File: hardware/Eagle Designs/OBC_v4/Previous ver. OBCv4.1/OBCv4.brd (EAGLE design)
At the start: 90.2 x 95.5 mm, 35 parts, among them J1 MOLEX_503763-0491MOLEX_503763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, J10 503763-0591, J11 503763-0591, J12 503763-0691, J13 MOLEX_503763-0291MOLEX_503763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, J16 U.FL-R-SMT-1(01), J2 MOLEX_503763-0491MOLEX_503763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, J6 MOLEX_503763-0491MOLEX_503763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, J9 U.FL-R-SMT-1(01), P8 SSW-123-02-G-D, P9 SSW-123-02-G-D, U1 TMP36FSZR_8_ADI-L, U2 LTC1477CS8LINEAR_TECHNOLOGY_L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, U3 RFM69HCW_433_900, U6 ORION_A38LORION_A38L, U7 PA1010D, X1 C25582-40G-M36-0A, X2 SSW-120-02-G-D

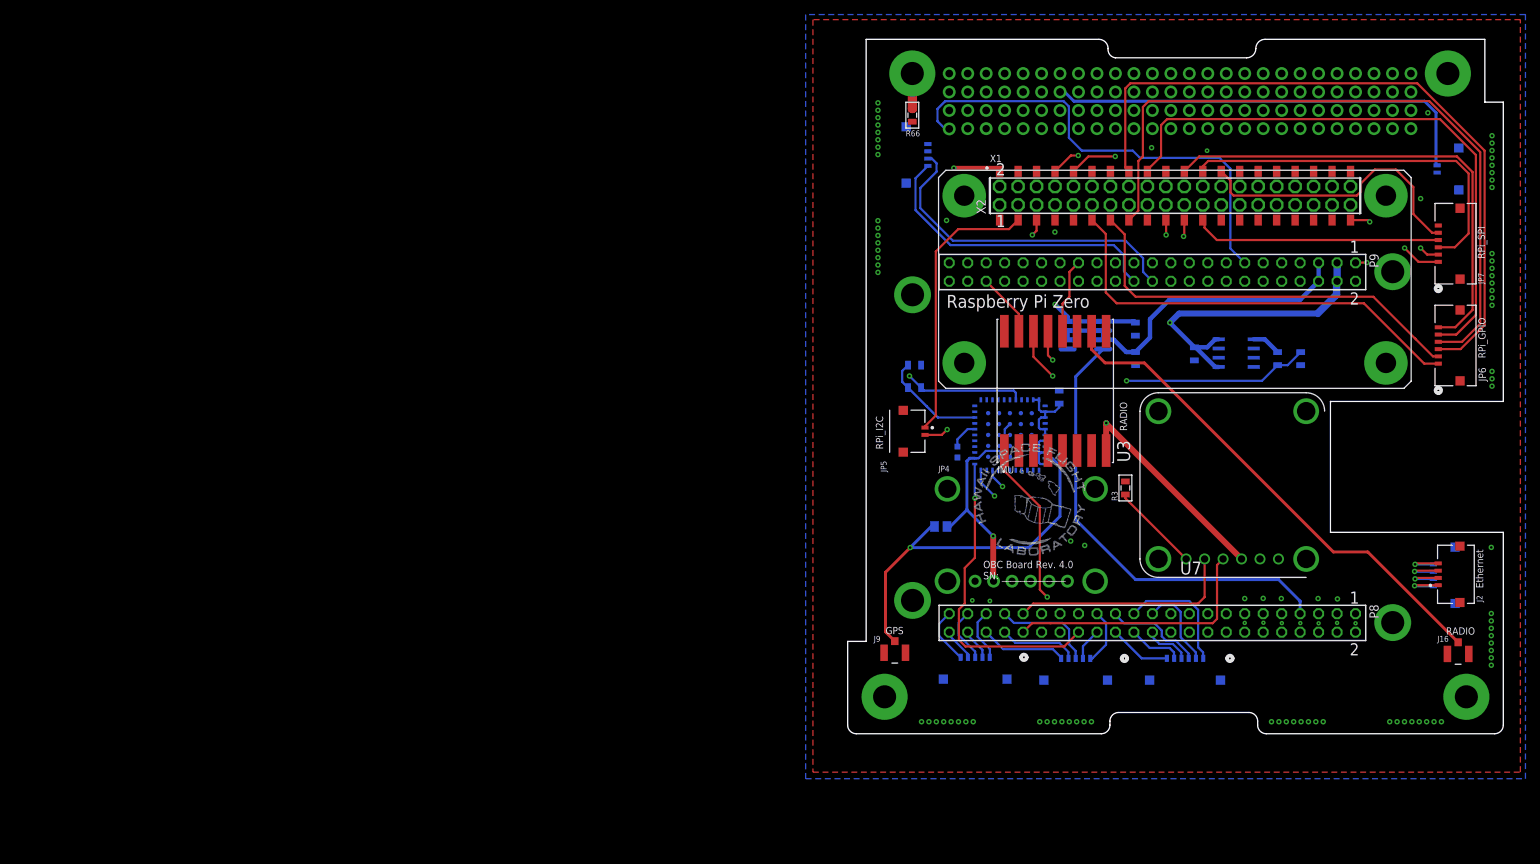
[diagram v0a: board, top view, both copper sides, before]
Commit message: updated OBC v4.1; verified & updated Battery Charging Circuit
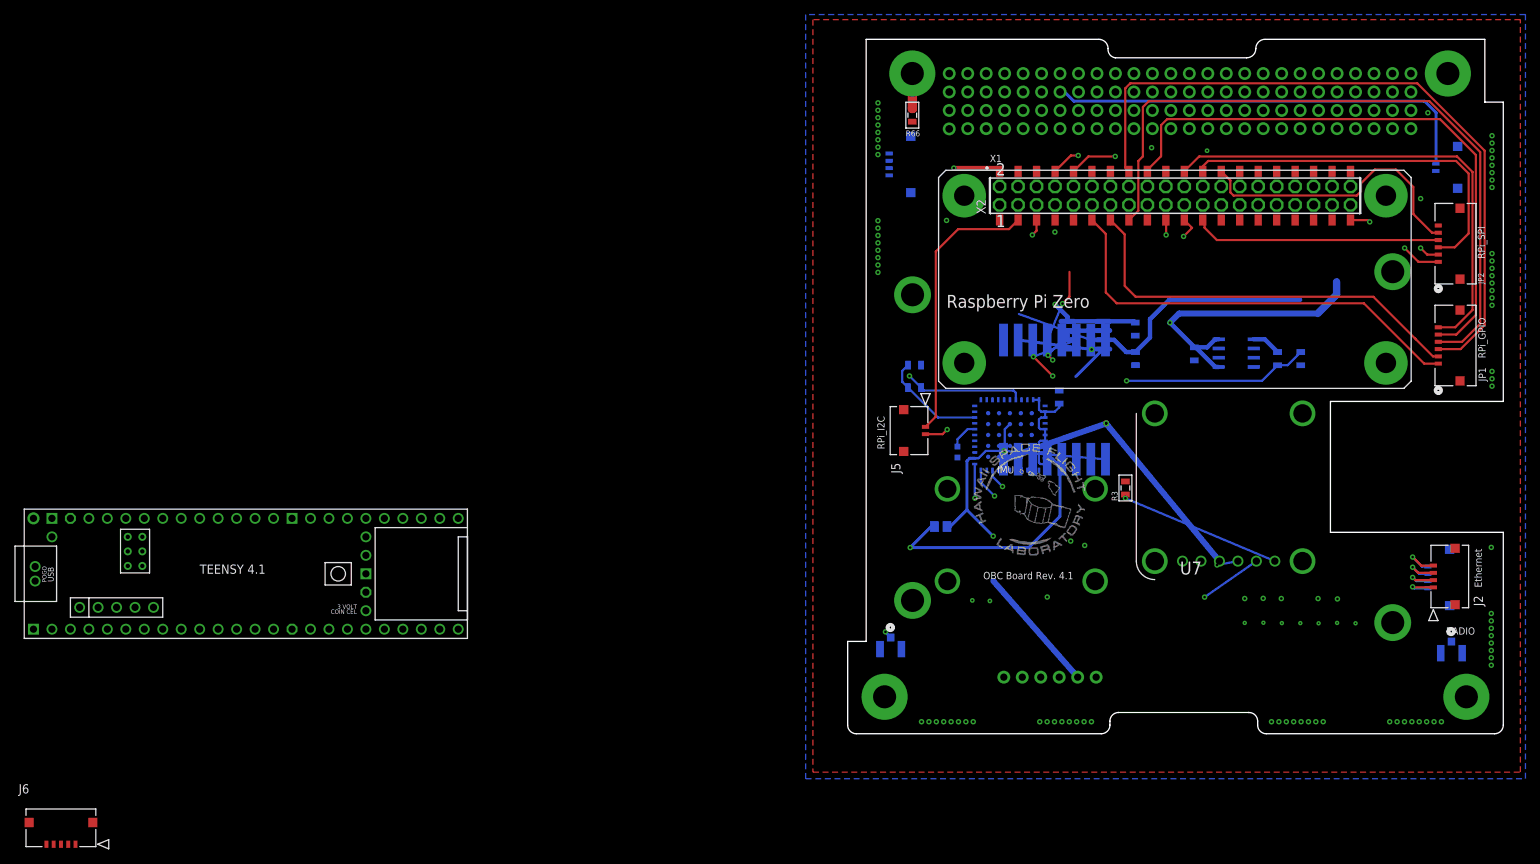
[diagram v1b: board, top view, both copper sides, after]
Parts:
- removed J10, J11: 503763-0591, Improved Molex 503763-0591:CONN_5037630591_MOL
- removed J12: 503763-0691, Improved Molex 503763-0691:CONN_503763-0691_MOL
- removed J13, JP5: MOLEX_503763-0291MOLEX_503763-0291_0_0, Molex - 503763-0291:MOLEX_503763-0291_0
- removed P8, P9: SSW-123-02-G-D, con-samtec:SSW-123-02-G-D
- added J3, J5: 5037630291, OBCv4:CON_5037630291
- added J4: 5037630491, OBCv4:CON_5037630491
- added U$1: TEENSY41, OBCv4:TEENSY41
- C1: value .1uF -> 0.1 uF
- C2, C3: value 1uF -> 1 uF
- J1, J2: value MOLEX_503763-0491MOLEX_503763-0491_0_0 -> 5037630491; device Molex - 503763-0491:MOLEX_503763-0491_0 -> OBCv4:CON_5037630491
- J6: value MOLEX_503763-0491MOLEX_503763-0491_0_0 -> 5037630591; device Molex - 503763-0491:MOLEX_503763-0491_0 -> OBCv4:CON_5037630591
- R1: value 27k -> 45.3k
- moved J6 148.9 mm to (-106.2, -15.2), flipped to the top, turned to 0 degrees
- moved JP4 13.8 mm to (27.8, 7.78), flipped to the bottom
- moved J2 3.58 mm to (80.6, 20.1)
- moved J1 3.42 mm to (79.8, 23.0)
- moved U3 1.20 mm to (28.4, 46.0), flipped to the bottom
- moved J16 0.93 mm to (83.0, 11.1), flipped to the bottom
- moved J9 0.75 mm to (5.92, 11.6), flipped to the bottom
- moved U7 0.58 mm to (52.4, 33.9), flipped to the bottom
- renumbered JP6 to JP1, JP7 to JP2
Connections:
- removed net AGND: P9.34
- removed net BUS_UART4_RXD(BBB_TX): H1.1.1, P9.13
- removed net BUS_UART4_TXD(BBB_RX): H1.1.2, P9.11
- removed net GPIO0_27: P8.17
- removed net GPIO1_0: J12.1, P8.25
- removed net GPIO1_1: J12.4, P8.24
- removed net GPIO1_12: P8.12
- removed net GPIO1_13: P8.11
- removed net GPIO1_14: P8.16
- removed net GPIO1_15: P8.15
- removed net GPIO1_16: P9.15
- removed net GPIO1_17: P9.23
- removed net GPIO1_2: P8.5
- removed net GPIO1_28: P9.12
- removed net GPIO1_29: J12.5, P8.26
- removed net GPIO1_3: P8.6
- removed net GPIO1_30: P8.21
- removed net GPIO1_31: P8.20
- removed net GPIO1_4: J12.2, P8.23
- removed net GPIO1_6: P8.3
- removed net GPIO1_7: P8.4
- removed net GPIO2_1: P8.18
- removed net GPIO2_10: J10.1, P8.41
- removed net GPIO2_11: J11.5, P8.42
- removed net GPIO2_12: J11.3, P8.39
- removed net GPIO2_13: J11.4, P8.40
- removed net GPIO2_22: J12.3, P8.27
- removed net GPIO2_23: J11.1, P8.29
- removed net GPIO2_24: J12.6, P8.28
- removed net GPIO2_25: J11.2, P8.30
- removed net GPIO2_6: J10.5, P8.45
- removed net GPIO2_7: J10.4, P8.46
- removed net GPIO2_8: J10.3, P8.43
- removed net GPIO2_9: J10.2, P8.44
- removed net GPIO3_19: P9.27
- removed net GPIO3_21: P9.25
- removed net GPIO_10: P8.31
- removed net SPI1_CS0: P9.28
- removed net SYS_RESET: P9.10
- removed net UART4_CTSN: P8.35
- removed net UART4_RTSN: P8.33
- new net I2C1_SCL: U$1.24-A10/TX6/SCL2
- new net I2C1_SDA: U$1.25-A11/RX6/SDA2
- new net N$19: U$1.3V3-2
- new net T_CS: U$1.10-CS\MQSR
- new net T_GPIO2: J6.1, U$1.2-OUT2
- new net T_GPIO3: J6.2, U$1.3-LRCLK2
- new net T_GPIO4: J6.3, U$1.4-BCLK2
- new net T_GPIO5: J6.4, U$1.5-IN2
- new net T_GPIO6: J6.5, U$1.6-OUT1D
- new net UART4_RXD: H1.1.1, U$1.16-A2/RX4/SCL1
- new net UART4_TXD: H1.1.2, U$1.17-A3/TX4/SDA1
- net +3V3_VCC: now also U$1.3V3-1, U$1.3V3-3; no longer P9.3, P9.4
- net +5V_VCC: now also U$1.+5V, U$1.VIN; no longer P9.5, P9.6
- net AIN0: now also U$1.14-A0/TX3/SPDIF_OUT; no longer P9.39
- net AIN1: now also U$1.15-A1/RX3/SPDIF_IN; no longer P9.40
- net AIN2: now also U$1.41-A17/MISO1; no longer P9.37
- net AIN3: now also U$1.20-A6/TX5/LRCLK1; no longer P9.38
- net AIN4: now also U$1.21-A7/RX5/BCLK1; no longer P9.33
- net AIN5: now also U$1.22-A8/CTX1; no longer P9.36
- net AIN6: now also U$1.23-A9/CRX1/MCLK1; no longer P9.35
- net GND: now also J3.2, J3.3, J3.4, J4.2, J4.4, J4.5, J4.6, J5.3, J5.4, J6.7, U$1.GND1, U$1.GND2, U$1.GND3, U$1.GND4, U$1.GND5, U$1.GND6; no longer J10.6, J10.7, J11.6, J11.7, J12.7, J12.8, J13.2, J13.3, J13.4, J6.3, J6.4, J6.5, JP5.3, JP5.4, P8.1, P8.2, P9.1, P9.2
- net GPS_RSTN: now also U$1.33-MCLK2; no longer P8.32
- net I2C2_SCL: now also U$1.19-A5/SCL0; no longer P9.19
- net I2C2_SDA: now also U$1.18-A4/SDA0; no longer P9.20
- net RADIO_RESET: now also U$1.7-RX2/OUT1A; no longer P8.36
- net RPI_ENABLE: now also U$1.36-PWM; no longer P8.7
- net SCL1_I2C: now also J5.2; no longer JP5.2
- net SDA1_I2C: now also J5.1; no longer JP5.1
- net SPI0_MISO: now also U$1.12-MISO/MQSL
- net SPI0_MOSI: now also U$1.11-MOSI/CTX1
- net SPI0_SCLK: now also U$1.13-SCK/LED
- net SPI1_CS1: now also U$1.38-A14/CS/IN1; no longer P9.42
- net SPI1_D0: now also U$1.39-A15/CS/OUT1A; no longer P9.29
- net SPI1_D1: now also U$1.26-A12/MOSI1; no longer P9.30
- net SPI1_SCLK: now also U$1.27-A13/SCK1; no longer P9.31
- net SW_5V_1: now also J3.1; no longer J13.1
- net UART1_RXD: now also J4.1, U$1.34-RX8; no longer J6.1, P9.26
- net UART1_TXD: now also J4.3, U$1.35-TX8; no longer J6.2, P9.24
- net UART2_RXD: now also U$1.0-RX1/CS1/CRX2; no longer P9.22
- net UART2_TXD: now also U$1.1-TX1/MISO1/CTX2; no longer P9.21
- net UART5_RXD: now also U$1.28-RX7; no longer P8.38
- net UART5_TXD: now also U$1.29-TX7; no longer P8.37
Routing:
- net BUS_UART4_RXD(BBB_TX): track 64.6 -> 0.00 mm
- net BUS_UART4_TXD(BBB_RX): track 60.9 -> 0.00 mm
- net N$12: track 69.6 -> 10.2 mm, vias 0 -> 1
- net RPI_ENABLE: track 62.3 -> 5.35 mm
- net UART1_TXD: track 45.7 -> 0.00 mm
- net UART1_RXD: track 42.2 -> 0.00 mm
- net GPS_RSTN: track 42.7 -> 4.70 mm
- net UART5_RXD: track 60.7 -> 25.8 mm, vias 1 -> 2
- net UART5_TXD: track 52.6 -> 29.8 mm, vias 1 -> 2
- net +3V3_VCC: track 142.8 -> 161.0 mm, vias 3 -> 4
- net GPIO1_0: track 17.0 -> 0.00 mm
- net GPIO2_12: track 14.1 -> 0.00 mm
- net N$17: track 51.1 -> 37.4 mm, vias 1 -> 2
- net GPIO2_22: track 13.5 -> 0.00 mm
- net I2C2_SDA: track 49.3 -> 62.3 mm
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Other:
- board text added: "OBC Board Rev. 4.1"
- board text removed: "OBC Board Rev. 4.0 SN: ______________"
